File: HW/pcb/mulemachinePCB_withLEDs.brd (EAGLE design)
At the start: 85.1 x 45.1 mm, 29 parts, among them IC1 LD117AV50, IC2 MEGA8-P, J1 DCJ0202, Q1 16Mhz

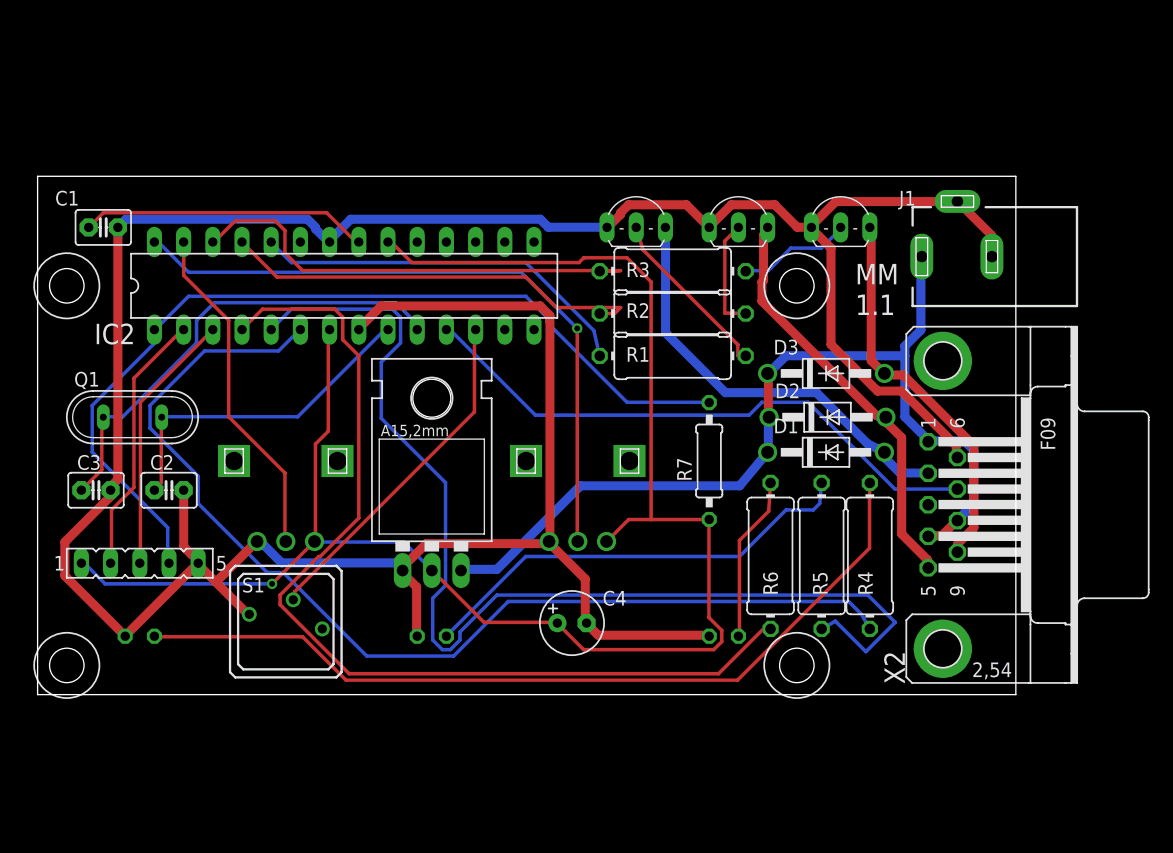
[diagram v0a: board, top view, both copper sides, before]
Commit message: preparing files for first prototype of version 1.0 of Mule Machine. Corrected Code to reflect Orange and Green LEDs being flipped on PCB and Code. Used PCB Version. Added some new design features to laser panel and PCB for version 1.1
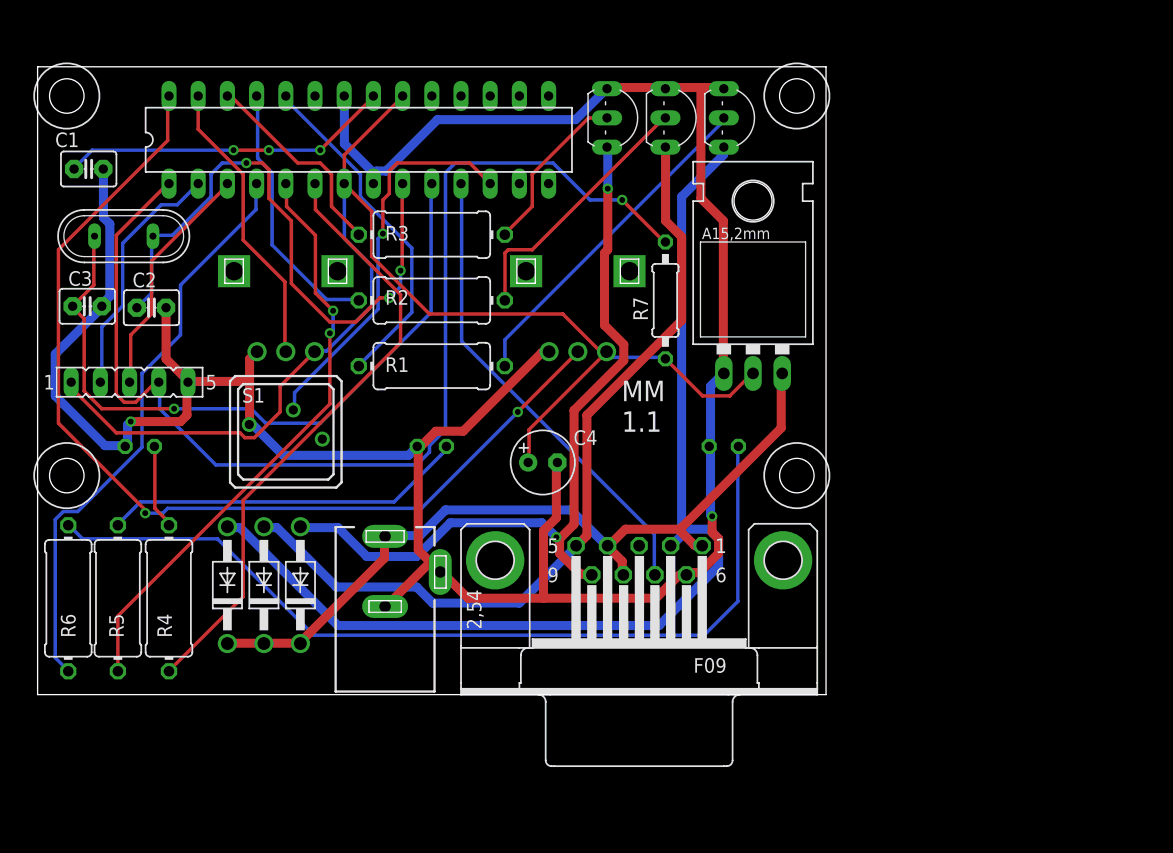
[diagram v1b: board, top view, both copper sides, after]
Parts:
- moved R5 61.3 mm to (6.99, 8.38)
- moved R6 61.2 mm to (2.67, 8.38)
- moved R4 61.1 mm to (11.4, 8.38)
- moved J1 56.8 mm to (30.2, 10.7), turned to 0 degrees
- moved D1 53.3 mm to (16.5, 9.53), turned to 90 degrees
- moved D2 51.2 mm to (19.7, 9.53), turned to 90 degrees
- moved D3 49.3 mm to (22.9, 9.53), turned to 90 degrees
- moved IC1 32.8 mm to (62.2, 31.8)
- moved X2 26.9 mm to (52.3, 11.7), turned to 180 degrees
- moved R3 21.2 mm to (34.3, 40.0)
- moved R2 21.0 mm to (34.3, 34.3)
- moved R1 21.0 mm to (34.3, 28.6)
- moved T3 20.8 mm to (50.8, 50.2), turned to 270 degrees
- moved LED1 16.5 mm to (8.89, 21.6)
- moved LED2 16.5 mm to (34.3, 21.6)
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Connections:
- net N$2 renamed ORANGELED
- net N$25 renamed ORANGE
- net N$26 renamed YELLOW
- net N$27 renamed GREEN
- net N$3 renamed YELLOWLED
- net N$4 renamed GREENLED
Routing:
- net ORANGE: track 74.2 -> 7.39 mm
- net GREEN: track 14.4 -> 76.9 mm
- net P1: track 37.2 -> 91.0 mm
- net YELLOWLED: track 96.5 -> 51.9 mm, vias 0 -> 2
- net ORANGELED: track 93.2 -> 53.8 mm
- net GND: track 270.2 -> 232.0 mm, vias 0 -> 2
- net GREENLED: track 85.6 -> 50.9 mm
- net P2: track 36.5 -> 71.1 mm
- net P3: track 33.5 -> 67.5 mm, vias 0 -> 2
- net 5V: track 147.3 -> 114.7 mm, vias 1 -> 0
- net SOURRPOT: track 58.5 -> 86.9 mm, vias 1 -> 2
- net N$12: track 29.4 -> 52.9 mm, vias 0 -> 3
- net N$23: track 41.0 -> 18.1 mm
- net RESET: track 79.1 -> 100.5 mm, vias 0 -> 1
- net N$11: track 41.0 -> 61.2 mm, vias 0 -> 1
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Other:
- board size 85.1 x 45.1 mm -> 68.6 x 54.6 mm

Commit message: fixed #13 with additional 100uF cap on 12V power line and 0.1uF cap on 5v line in parallel with 470uF cap. This smooths the 12V line and the 5V line for more powerful motors. needs more duration of bootup time to get caps charged, but can run Mixing Mode with full strength and sourness settings for > 5 minutes. Tested on V1.0 PCB. Implemented caps into V1.1 PCB and re-autorouted.
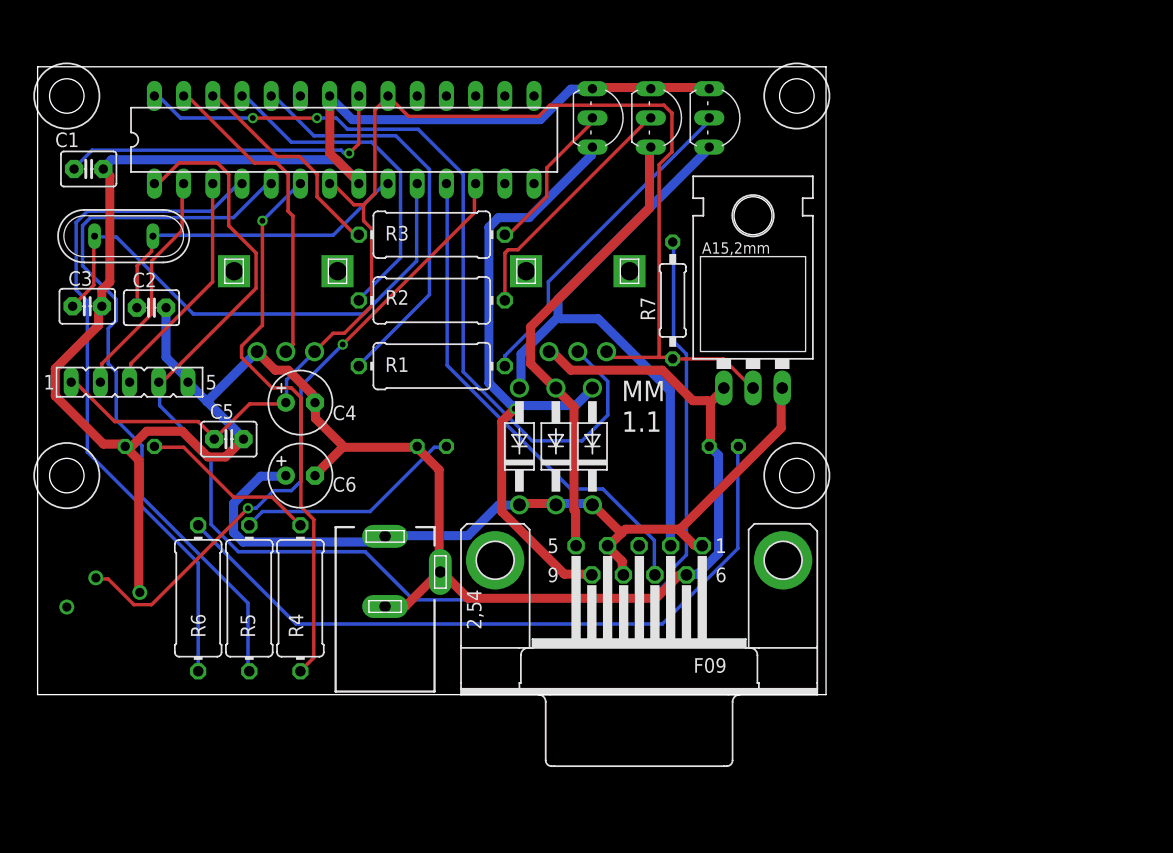
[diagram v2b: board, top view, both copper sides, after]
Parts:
- added C5: 0.1uF, capacitor-wima:C2.5-3
- added C6: 100uF, rcl:E2,5-6
- moved D2 28.1 mm to (45.1, 21.6)
- moved D3 28.1 mm to (48.3, 21.6)
- moved D1 28.1 mm to (41.9, 21.6)
- moved C4 21.7 mm to (22.9, 25.4)
- moved S1 21.6 mm to (5.71, 8.26), flipped to the bottom
- moved R4 11.4 mm to (22.9, 8.38)
- moved R5 11.4 mm to (18.4, 8.38)
- moved R6 11.3 mm to (14.0, 8.38)
- moved T1 1.27 mm to (59.7, 50.2)
- moved T2 1.27 mm to (54.6, 50.2)
- moved IC1 1.27 mm to (62.2, 30.5)
- moved IC2 1.27 mm to (26.7, 48.3)
- moved T3 1.27 mm to (49.5, 50.2)
- moved R7 0.63 mm to (55.2, 34.3)
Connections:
- net 5V: now also C5.1
- net GND: now also C5.2, C6.-
- net VCC: now also C6.+
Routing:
- net P1: track 91.0 -> 53.7 mm
- net P2: track 71.1 -> 40.7 mm
- net N$12: track 52.9 -> 29.2 mm, vias 3 -> 0
- net N$24: track 34.1 -> 55.5 mm, vias 1 -> 2
- net RESET: track 100.5 -> 118.4 mm, vias 1 -> 0
- net SOURRPOT: track 86.9 -> 69.5 mm
- net N$11: track 61.2 -> 46.4 mm, vias 1 -> 0
- net GREEN: track 76.9 -> 62.1 mm
- net YELLOW: track 31.6 -> 20.0 mm
- net YELLOWLED: track 51.9 -> 63.3 mm, vias 2 -> 0
- net P3: track 67.5 -> 56.1 mm, vias 2 -> 1
- net GND: track 232.0 -> 240.8 mm, vias 2 -> 0
- net GREENLED: track 50.9 -> 59.3 mm
- net ORANGE: track 7.39 -> 15.6 mm
- net N$22: track 23.1 -> 29.3 mm
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
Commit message: sourced push button and added to schematic and PCB layout. matched needed mounting to laser front panel cutout.
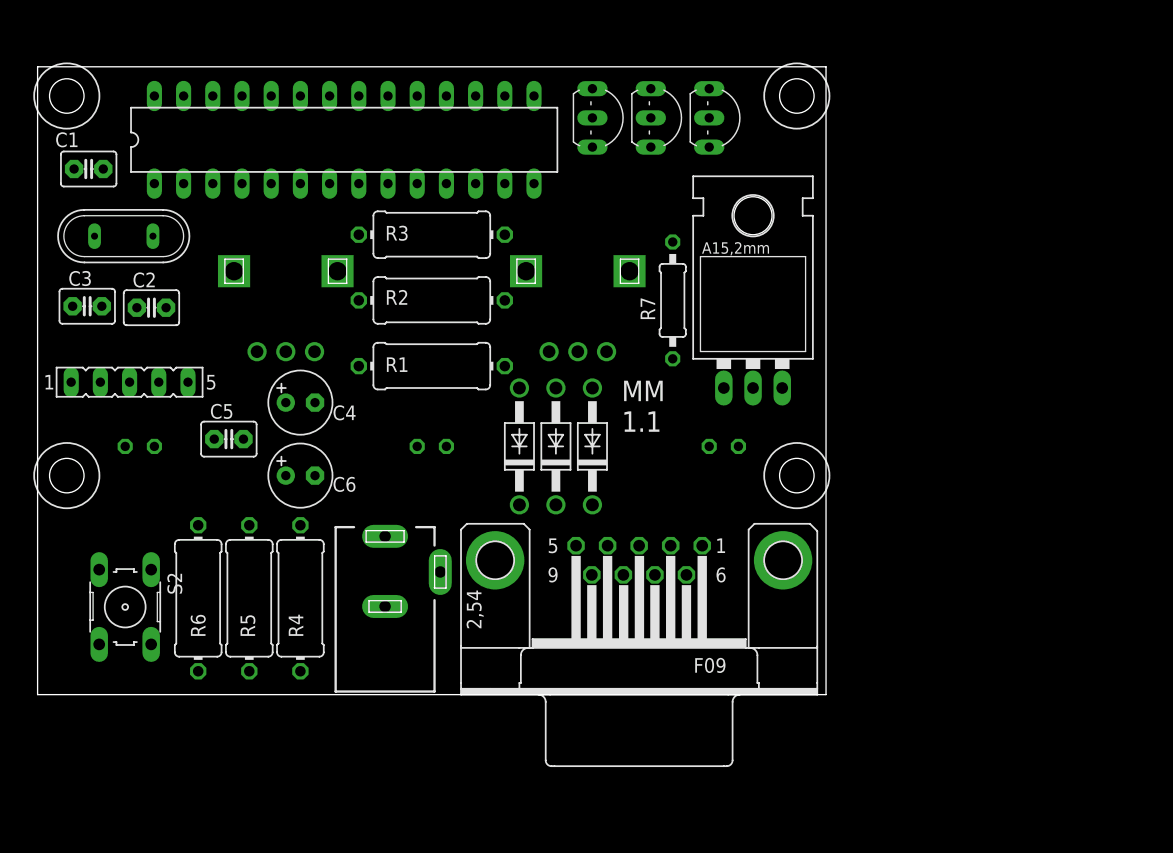
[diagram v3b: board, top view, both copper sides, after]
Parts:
- removed S1: RDT1034, switch:RDT1034
- added S2: (no value), switch-omron:B3F-10XX
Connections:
- net GND: now also S2.3, S2.4; no longer S1.A1
- net N$24: now also S2.1, S2.2; no longer S1.B
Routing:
- net GND: track 240.8 -> 0.00 mm
- net 5V: track 119.3 -> 0.00 mm
- net RESET: track 118.4 -> 0.00 mm
- net VCC: track 73.4 -> 0.00 mm
- net SOURRPOT: track 69.5 -> 0.00 mm, vias 2 -> 0
- net YELLOWLED: track 63.3 -> 0.00 mm
- net GREEN: track 62.1 -> 0.00 mm
- net GREENLED: track 59.3 -> 0.00 mm
- net P3: track 56.1 -> 0.00 mm, vias 1 -> 0
- net N$24: track 55.5 -> 0.00 mm, vias 2 -> 0
- net P1: track 53.7 -> 0.00 mm
- net ORANGELED: track 48.6 -> 0.00 mm, vias 1 -> 0
- net N$11: track 46.4 -> 0.00 mm
- net CUPSENSOR: track 43.2 -> 0.00 mm
- net P2: track 40.7 -> 0.00 mm
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
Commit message: finished mating between front panel and PCB. routed PCB. PCB v1.1 is ready for gerber file generation and order.
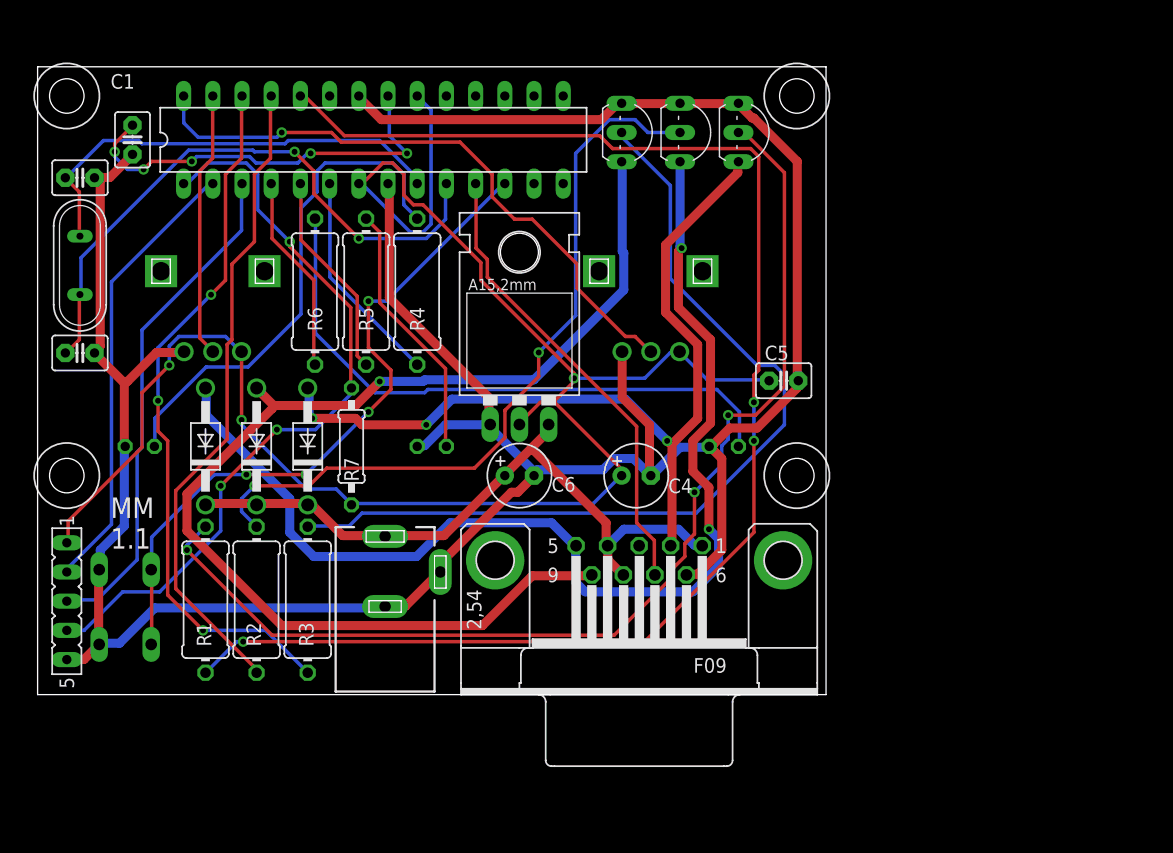
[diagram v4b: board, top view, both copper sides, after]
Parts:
- moved C5 48.5 mm to (64.9, 27.3)
- moved R3 33.5 mm to (23.5, 8.26), turned to 90 degrees
- moved R7 30.7 mm to (27.3, 21.6)
- moved D2 30.5 mm to (14.6, 21.6)
- moved R2 30.2 mm to (19.1, 8.26), turned to 90 degrees
- moved C4 29.9 mm to (52.1, 19.1)
- moved D3 29.2 mm to (19.1, 21.6)
- moved R4 28.5 mm to (33.0, 35.1)
- moved R5 28.5 mm to (28.6, 35.1)
- moved R6 28.5 mm to (24.1, 35.1)
- moved R1 28.3 mm to (14.6, 8.26), turned to 90 degrees
- moved IC1 20.6 mm to (41.9, 27.3)
- moved SV1 19.8 mm to (2.54, 8.13), turned to 270 degrees
- moved C6 19.0 mm to (41.9, 19.1)
- moved D1 18.4 mm to (23.5, 21.6)
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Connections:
- removed net N$24: IC2.12, S2.1, S2.2
- new net MANUALOVERRIDE: IC2.12, S2.3, S2.4
- net GND: now also S2.1, S2.2; no longer S2.3, S2.4
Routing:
- net GND: track 0.00 -> 253.4 mm
- net 5V: track 0.00 -> 155.3 mm, vias 0 -> 3
- net N$1: track 0.00 -> 127.7 mm, vias 0 -> 3
- net P3: track 0.00 -> 102.5 mm, vias 0 -> 1
- net P2: track 0.00 -> 98.3 mm, vias 0 -> 2
- net N$10: track 0.00 -> 96.1 mm, vias 0 -> 3
- net N$5: track 0.00 -> 77.3 mm
- net P1: track 0.00 -> 75.0 mm, vias 0 -> 3
- net N$6: track 0.00 -> 66.1 mm, vias 0 -> 2
- net RESET: track 0.00 -> 65.7 mm, vias 0 -> 3
- net N$23: track 0.00 -> 61.8 mm, vias 0 -> 3
- net MANUALOVERRIDE: track 0.00 -> 60.1 mm, vias 0 -> 4
- net VCC: track 0.00 -> 59.3 mm
- net N$22: track 0.00 -> 56.5 mm
- net SOURRPOT: track 0.00 -> 53.9 mm, vias 0 -> 1
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
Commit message: changed 12V side cap C6 to 470uF. rerouted board
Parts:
- added C7: 0.1uF, capacitor-wima:C2.5-3
- C6: value 100uF -> 470uF
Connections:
- net GND: now also C7.2
- net VCC: now also C7.1
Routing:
- net N$1: track 127.7 -> 64.3 mm, vias 3 -> 2
- net MANUALOVERRIDE: track 60.1 -> 93.3 mm, vias 4 -> 3
- net P1: track 75.0 -> 100.9 mm, vias 3 -> 5
- net VCC: track 59.3 -> 84.5 mm, vias 0 -> 1
- net N$11: track 52.6 -> 76.4 mm, vias 2 -> 5
- net N$10: track 96.1 -> 77.0 mm, vias 3 -> 5
- net N$5: track 77.3 -> 59.1 mm, vias 0 -> 2
- net 5V: track 155.3 -> 172.1 mm
- net P2: track 98.3 -> 114.2 mm
- net N$6: track 66.1 -> 80.4 mm, vias 2 -> 0
- net GND: track 253.4 -> 239.9 mm
- net P3: track 102.5 -> 113.3 mm
- net N$13: track 36.0 -> 25.5 mm, vias 5 -> 3
- net N$22: track 56.5 -> 52.8 mm
- net N$23: track 61.8 -> 58.5 mm, vias 3 -> 5
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
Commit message: added decoupling cap for MCU to schematic. organized schematic with groups
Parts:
- added C8: 0.1uF, capacitor-wima:C2.5-3
- R1, R2, R3: value 150 -> 150R
- R4, R5, R6: value 200 -> 200R
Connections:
- net GREENLED renamed LED_GREEN
- net N$1 renamed PUMP_VODKA
- net N$22 renamed PUMP_GB
- net N$23 renamed PUMP_LIME
- net ORANGELED renamed LED_ORANGE
- net P1 renamed PUMP_VODKA_VCC
- net P2 renamed PUMP_GB_VCC
- net P3 renamed PUMP_LIME_VCC
- net YELLOWLED renamed LED_YELLOW
- net 5V: now also C8.2
- net GND: now also C8.1
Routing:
- net PUMP_VODKA_VCC: track 100.9 -> 54.1 mm, vias 5 -> 1
- net LED_ORANGE: track 18.9 -> 0.00 mm
- net LED_YELLOW: track 18.1 -> 0.00 mm
- net LED_GREEN: track 17.4 -> 0.00 mm
- net PUMP_GB_VCC: track 114.2 -> 111.2 mm
- net VCC: track 84.5 -> 83.7 mm
- net 5V: track 172.1 -> 171.4 mm
